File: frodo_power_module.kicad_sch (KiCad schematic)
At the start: 76 parts, among them J1 Conn_01x06, J1 Keystone 1048, J10 SWD Header, J2 Conn_01x06, J3 Conn_01x04, J4 Molex MicroFit 2x2, J5 JST-GH, J6 JST-GH, U1 STM32F042F6Px, U2 L7805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

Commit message: Add review comments
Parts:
- removed J3: Conn_01x04, symbol Connector_Generic:Conn_01x04
- removed R2, R27: 100, Resistor_SMD:R_0603_1608Metric, symbol Device:R_Small
- added J4: Molex MicroFit 2x2, Connector_Molex:Molex_Micro-Fit_3.0_43045-0400_2x02_P3.00mm_Horizontal, symbol Connector_Generic:Conn_01x04
- J1, J2: value Conn_01x06 -> Molex MicroFit 2x3
- R7: value 220 -> 1k; LCSC# C107696 -> (none); Manufacturer YAGEO -> (none); Part# RC0603FR-07220RL -> (none)
- R8: value 120 -> 680; LCSC# C107696 -> (none); Manufacturer YAGEO -> (none); Part# RC0603FR-07220RL -> (none)
- renumbered J4 to J3, JP2 to JP1, JP1 to JP2
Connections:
- net +VSW: now also J4.3 (Pin_3), J4.4 (Pin_4)
- net GND: now also R7.2, R8.2, J4.1 (Pin_1), J4.2 (Pin_2)
- net at R7.1, U4.2 (ISET): now also R8.1
- net at J6.1 (Pin_1): no longer J5.1 (Pin_1)
- no-connect marks 1 -> 3
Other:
- note added: "ISET: ~405 = ~740mA"
- note added: "REVIEW: - adjusted Iset resistors to use only 2 resistors"
- note added: "REVIEW: - flipped connector symbols for MicroFit connectors so 1 (GND) is on the bottom - slightly rearranged CAN bus layout - adjusted jumper numbering"
- note added: "TODO: pull STAT1/2 up to VDC, limit voltage to uC"
- note removed: "ISET: 390 = 800mA"
- moved on the sheet: D3, J1, J2, J3, J5, J6, JP2, JP3, R26, R7, R8

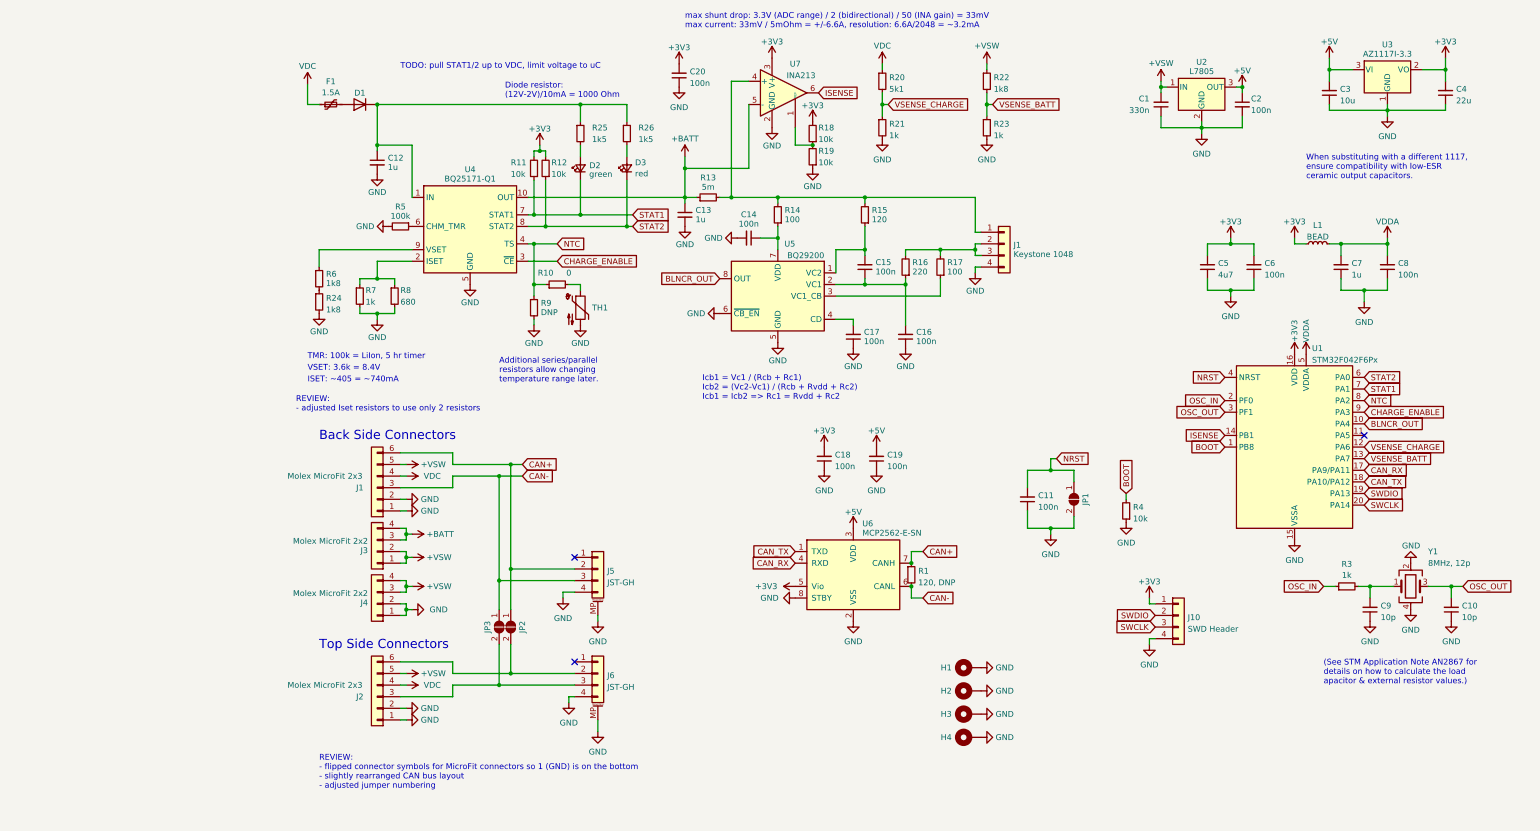
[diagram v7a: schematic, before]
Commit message: Review: Added resistor-zener diode network to limit voltage to STAT1/2 to ~3.3V
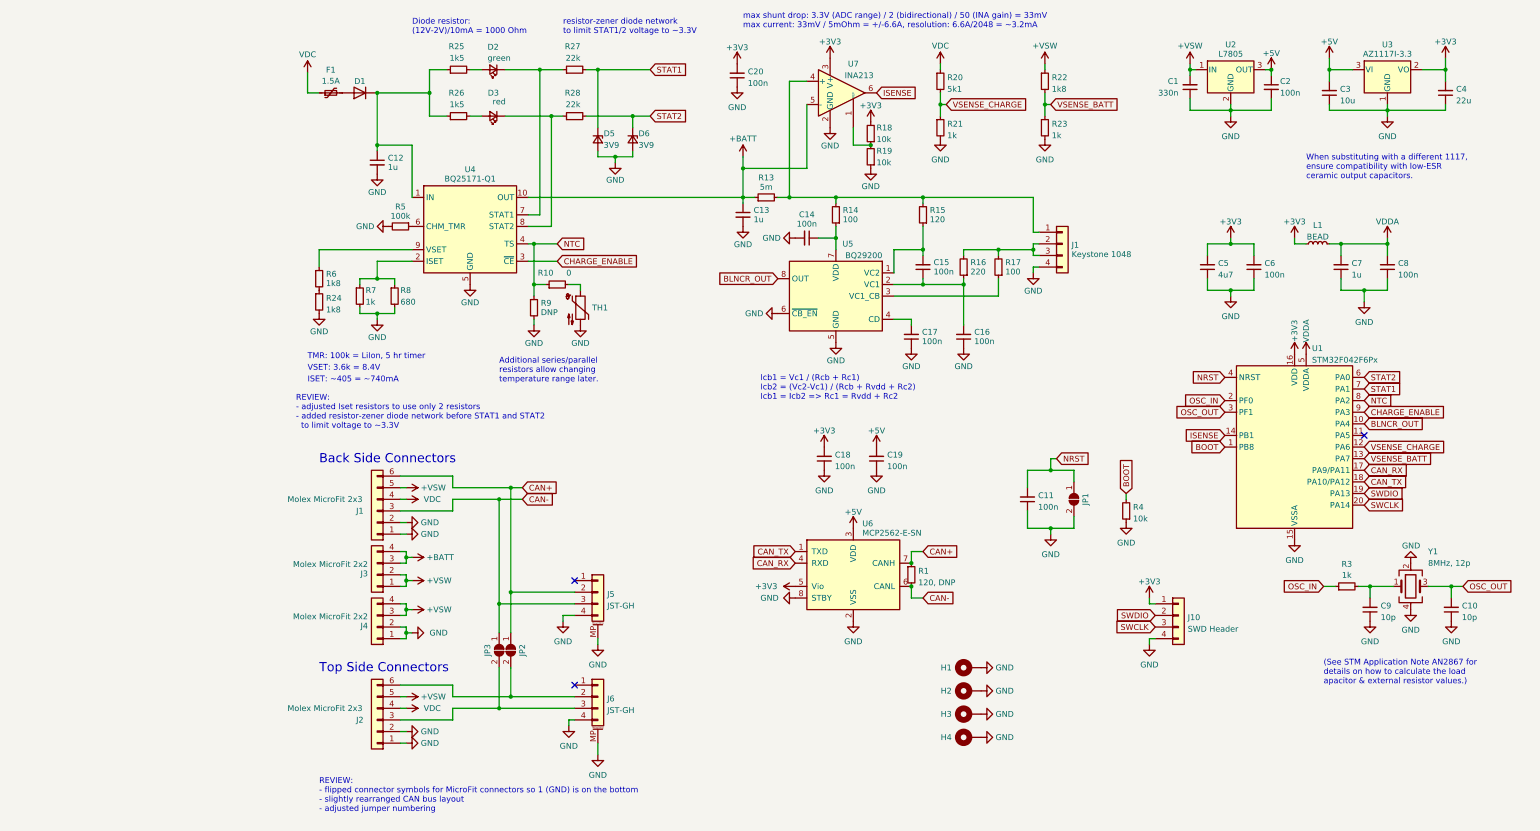
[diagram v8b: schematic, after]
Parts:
- removed R11, R12: 10k, Resistor_SMD:R_0603_1608Metric, symbol Device:R_Small
- added D5, D6: 3V9, symbol Device:D_Zener_Small
- added R27, R28: 22k, Resistor_SMD:R_0603_1608Metric, symbol Device:R_Small
- D2: renamed from D3; value red -> green
- D3: renamed from D2; value green -> red
- renumbered R26 to R25, R25 to R26
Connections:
- net GND: now also D5.2 (A), D6.2 (A)
- net STAT1: now also D5.1 (K), R27.2; no longer D3.1 (K), U4.7 (STAT1)
- net STAT2: now also D6.1 (K), R28.2; no longer D2.1 (K), U4.8 (STAT2)
- new net: D3.1 (K), R28.1, U4.8 (STAT2)
- new net: D2.1 (K), R27.1, U4.7 (STAT1)
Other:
- note added: "REVIEW: - adjusted Iset resistors to use only 2 resistors - added resistor-zener diode network before STAT1 and STAT2 to limit voltage to ~3.3V"
- note added: "resistor-zener diode network to limit STAT1/2 voltage to ~3.3V"
- note removed: "REVIEW: - adjusted Iset resistors to use only 2 resistors"
- note removed: "TODO: pull STAT1/2 up to VDC, limit voltage to uC"
- moved on the sheet: C1, C13, C14, C15, C16, C17, C2, C20, D1, D2, D3, F1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
